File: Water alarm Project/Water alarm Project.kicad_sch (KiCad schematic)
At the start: 8 parts, among them J1 Jack-DC, J2 Screw_Terminal_01x02, Q1 2N7000

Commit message: I worked on the pcb file for hours to find the kicad to crash and lost all my pcb files
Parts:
- added D1: LED_Small_Filled, LED_THT:LED_D4.0mm, symbol Device:LED_Small_Filled
- added R2: 6.8k, Resistor_THT:R_Axial_DIN0204_L3.6mm_D1.6mm_P5.08mm_Horizontal, symbol Device:R_Small_US
- BZ1: value (none) -> Buzzer; footprint (none) -> Buzzers:Buzzer_D30mm_H20mm_P15mm__668-1652-ND__AI-3035-TT-12V-R; DKPN (none) -> 668-1652-ND
- C1: footprint (none) -> Capacitor_THT:C_Disc_D3.0mm_W1.6mm_P2.50mm; DKPN (none) -> 56-K102K10X7RH5UL2CT-ND
- J1: footprint (none) -> Connector_BarrelJack:BarrelJack_GCT_DCJ200-10-A_Horizontal; DKPN (none) -> CP-037A-ND
- J2: footprint (none) -> TerminalBlock_Phoenix:TerminalBlock_Phoenix_PT-1,5-2-5.0-H_1x02_P5.00mm_Horizontal; DKPN (none) -> 2057-EBAA-02-C-ND
- Q1: DKPN (none) -> 4878-2N7000CT-ND
- R1: footprint (none) -> Resistor_THT:R_Axial_DIN0204_L3.6mm_D1.6mm_P5.08mm_Horizontal; DKPN (none) -> CF18JT10M0CT-ND
- Z1: DKPN (none) -> 364-1254-ND
- Z2: DKPN (none) -> 1927-1053-ND
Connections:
- net GND: now also R2.2
- net VCC: now also D1.2 (A)
- new net: D1.1 (K), R2.1

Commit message: Added gerber files and plots
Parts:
- D1: DKPN (none) -> CF18Jt6k80CT-ND
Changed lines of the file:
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@@
+			)
+		)
+		(property "DKPN" "CF18Jt6k80CT-ND"
+			(at 148.59 55.88 90)
+			(hide yes)
+			(show_name no)
+			(do_not_autoplace no)
+			(effects
+				(font
+					(size 1.27 1.27)
+				)
 			)
 		)

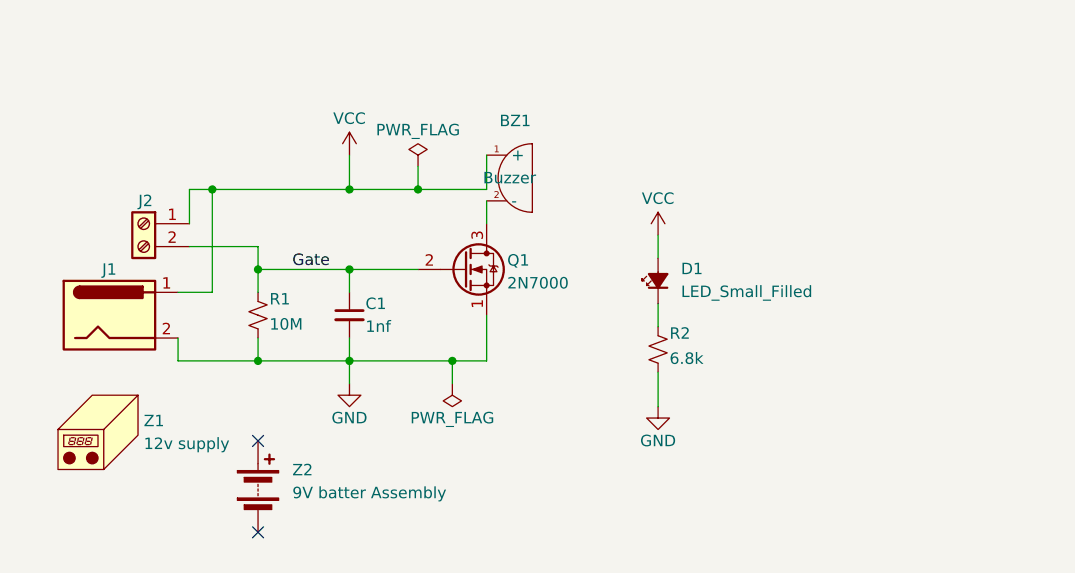
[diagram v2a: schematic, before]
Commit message: Updated the Water alarm added new parts
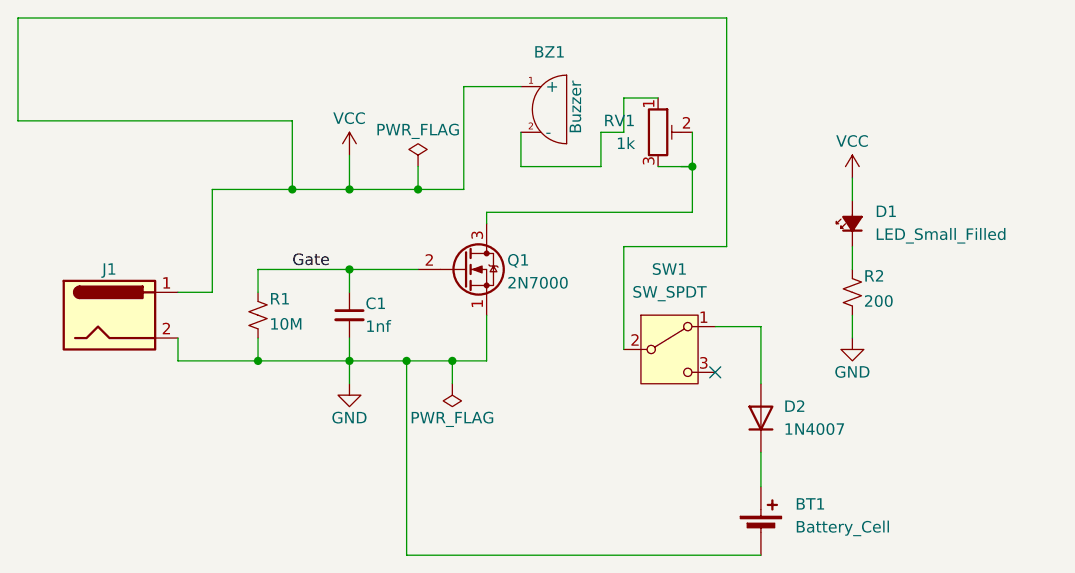
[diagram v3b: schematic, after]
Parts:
- removed J2: Screw_Terminal_01x02, TerminalBlock_Phoenix:TerminalBlock_Phoenix_PT-1,5-2-5.0-H_1x02_P5.00mm_Horizontal, symbol Connector:Screw_Terminal_01x02
- removed Z1: 12v supply, symbol Mechanical:Housing
- removed Z2: 9V batter Assembly, symbol Device:Battery
- added BT1: Battery_Cell, Battery:BatteryHolder_Keystone_103_1x20mm, symbol Device:Battery_Cell
- added D2: 1N4007, Diode_THT:D_DO-41_SOD81_P10.16mm_Horizontal, symbol Diode:1N4007
- added RV1: 1k, Potentiometer_THT:Potentiometer_Bourns_3339P_Vertical_HandSoldering, symbol Device:R_Potentiometer_Trim
- added SW1: SW_SPDT, Button_Switch_THT:SW_Slide_SPDT_Straight_CK_OS102011MS2Q, symbol Switch:SW_SPDT
- D1: DKPN CF18Jt6k80CT-ND -> 67-1102-ND
- R2: value 6.8k -> 200; DKPN CF18JT10M0CT-ND -> CF14JT200RCT-ND
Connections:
- net GND: now also BT1.2 (-)
- net VCC: now also SW1.2 (B)
- net at BZ1.2 (-): now also RV1.1; no longer Q1.3 (D)
- new net: BT1.1 (+), D2.1 (K)
- new net: D2.2 (A), SW1.1 (A)
- new net: Q1.3 (D), RV1.2, RV1.3
- no-connect marks 2 -> 1
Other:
- moved on the sheet: BZ1, D1, R2
